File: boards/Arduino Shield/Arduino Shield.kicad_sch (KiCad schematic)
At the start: 21 parts, among them J1 Screw_Terminal_01x08, J11 Screw_Terminal_01x08, J12 Screw_Terminal_01x06, J2 Screw_Terminal_01x08, J3 Screw_Terminal_01x08, J4 Screw_Terminal_01x08, J5 Screw_Terminal_01x08, J6 Screw_Terminal_01x08, J7 Screw_Terminal_01x08, J9 Screw_Terminal_01x10, U1 A000062

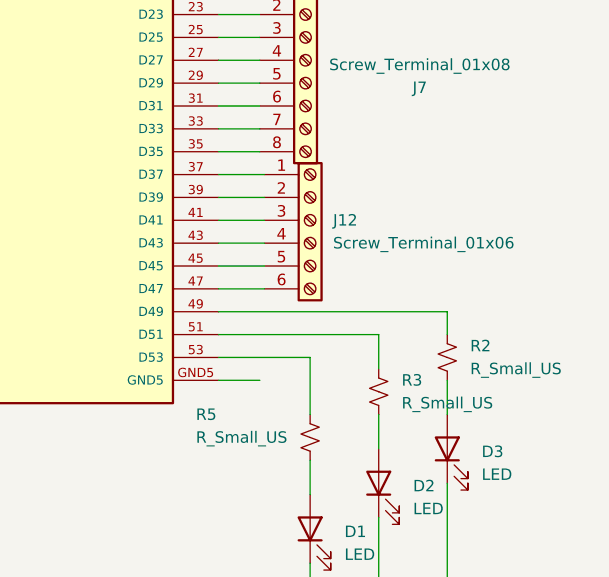
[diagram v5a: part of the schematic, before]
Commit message: Added LEDs and Ground
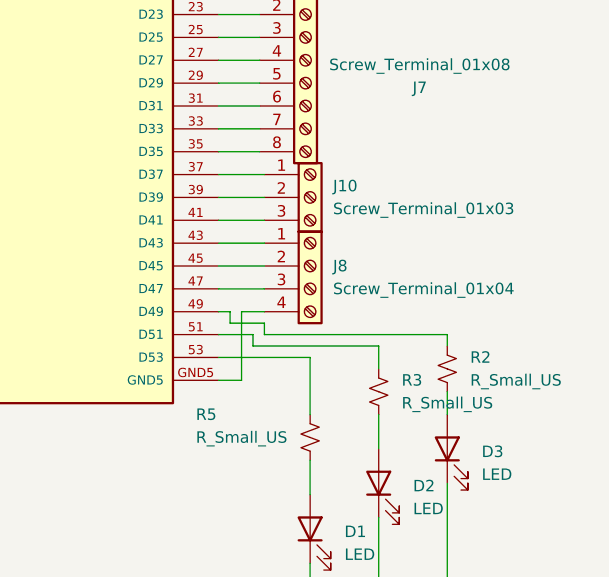
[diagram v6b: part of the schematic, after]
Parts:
- removed J12: Screw_Terminal_01x06, symbol Connector:Screw_Terminal_01x06
- added J10: Screw_Terminal_01x03, symbol Connector:Screw_Terminal_01x03
- added J8: Screw_Terminal_01x04, symbol Connector:Screw_Terminal_01x04
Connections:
- net at U1.37 (D37): now also J10.1 (Pin_1)
- net at U1.39 (D39): now also J10.2 (Pin_2)
- net at U1.41 (D41): now also J10.3 (Pin_3)
- net at U1.43 (D43): now also J8.1 (Pin_1)
- net at U1.45 (D45): now also J8.2 (Pin_2)
- net at U1.47 (D47): now also J8.3 (Pin_3)
- net at U1.GND5: now also J8.4 (Pin_4)
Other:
- moved on the sheet: R2
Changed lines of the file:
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@@
+    (stroke (width 0) (type default))
+  )
+  (wire (pts (xy 148.59 137.16) (xy 148.59 138.43))
     (stroke (width 0) (type default))
   )
@@
     (stroke (width 0) (type default))
   )
+  (wire (pts (xy 149.86 137.16) (xy 170.18 137.16))
+    (stroke (width 0) (type default))
+  )
   (wire (pts (xy 84.328 114.3) (xy 88.9 114.3))
     (stroke (width 0) (type default))
@@
     (stroke (width 0) (type default))
   )
-  (wire (pts (xy 144.78 134.62) (xy 170.18 134.62))
-    (stroke (width 0) (type default))
-  )
   (wire (pts (xy 85.09 137.16) (xy 85.09 143.51))
     (stroke (width 0) (type default))
@@
     (stroke (width 0) (type default))
   )
+  (wire (pts (xy 149.86 135.89) (xy 149.86 137.16))
+    (stroke (width 0) (type default))
+  )
+  (wire (pts (xy 147.32 134.62) (xy 149.86 134.62))
+    (stroke (width 0) (type default))
+  )
   (wire (pts (xy 83.82 142.24) (xy 83.82 137.16))
     (stroke (width 0) (type default))
@@
     (stroke (width 0) (type default))
   )
+  (wire (pts (xy 146.05 135.89) (xy 149.86 135.89))
+    (stroke (width 0) (type default))
+  )
   (wire (pts (xy 149.352 76.2) (xy 144.78 76.2))
     (stroke (width 0) (type default))
@@
     (stroke (width 0) (type default))
   )
-  (wire (pts (xy 144.78 142.24) (xy 149.352 142.24))
-    (stroke (width 0) (type default))
-  )
   (wire (pts (xy 144.78 129.54) (xy 149.86 129.54))
     (stroke (width 0) (type default))
@@
     (stroke (width 0) (type default))
   )
+  (wire (pts (xy 146.05 134.62) (xy 146.05 135.89))
+    (stroke (width 0) (type default))
+  )
   (wire (pts (xy 84.328 101.6) (xy 88.9 101.6))
     (stroke (width 0) (type default))
@@
     (stroke (width 0) (type default))
   )
+  (wire (pts (xy 148.59 138.43) (xy 162.56 138.43))
+    (stroke (width 0) (type default))
+  )
   (wire (pts (xy 84.328 93.98) (xy 88.9 93.98))
     (stroke (width 0) (type default))
@@
     (stroke (width 0) (type default))
   )
+  (wire (pts (xy 162.56 138.43) (xy 162.56 140.97))
+    (stroke (width 0) (type default))
+  )
+  (wire (pts (xy 147.32 142.24) (xy 147.32 134.62))
+    (stroke (width 0) (type default))
+  )
   (wire (pts (xy 84.328 38.1) (xy 88.9 38.1))
     (stroke (width 0) (type default))
@@
     (stroke (width 0) (type default))
   )
-  (wire (pts (xy 162.56 137.16) (xy 162.56 140.97))
+  (wire (pts (xy 144.78 134.62) (xy 146.05 134.62))
+    (stroke (width 0) (type default))
+  )
+  (wire (pts (xy 144.78 142.24) (xy 147.32 142.24))
+    (stroke (width 0) (type default))
+  )
+  (wire (pts (xy 170.18 137.16) (xy 170.18 138.43))
     (stroke (width 0) (type default))
   )
@@
     (stroke (width 0) (type default))
   )
-  (wire (pts (xy 144.78 137.16) (xy 162.56 137.16))
-    (stroke (width 0) (type default))
-  )
   (wire (pts (xy 84.328 35.56) (xy 88.9 35.56))
     (stroke (width 0) (type default))
@@
     (stroke (width 0) (type default))
   )
+  (wire (pts (xy 144.78 137.16) (xy 148.59 137.16))
+    (stroke (width 0) (type default))
+  )
   (wire (pts (xy 144.78 132.08) (xy 149.86 132.08))
     (stroke (width 0) (type default))
   )
-  (wire (pts (xy 170.18 142.24) (xy 170.18 146.05))
+  (wire (pts (xy 170.18 143.51) (xy 170.18 146.05))
     (stroke (width 0) (type default))
   )
@@
   )
   (wire (pts (xy 149.352 93.98) (xy 144.78 93.98))
-    (stroke (width 0) (type default))
-  )
-  (wire (pts (xy 170.18 134.62) (xy 170.18 137.16))
     (stroke (width 0) (type default))
   )
@@
     )
   )
+  (symbol (lib_id "Connector:Screw_Terminal_01x04") (at 154.94 129.54 0) (unit 1)
+    (in_bom yes) (on_board yes) (dnp no) (fields_autoplaced)
+    (property "Reference" "J8" (at 157.48 129.54 0)
+      (effects (font (size 1.27 1.27)) (justify left))
+    )
+    (property "Value" "Screw_Terminal_01x04" (at 157.48 132.08 0)
+      (effects (font (size 1.27 1.27)) (justify left))
+    )
+    (property "Footprint" "" (at 154.94 129.54 0)
+      (effects (font (size 1.27 1.27)) hide)
+    )
+    (property "Datasheet" "~" (at 154.94 129.54 0)
+      (effects (font (size 1.27 1.27)) hide)
+    )
+    (pin "1")
+    (pin "2")
+    (pin "3")
+    (pin "4")
+    (instances
+      (project "Arduino Shield"
+        (path "/d32bdb2e-fa3a-461a-9e34-c0053c91b5d5"
+          (reference "J8") (unit 1)
+        )
+      )
+    )
+  )
   (symbol (lib_id "Connector:Screw_Terminal_01x08") (at 79.248 86.36 180) (unit 1)
     (in_bom yes) (on_board yes) (dnp no)
@@
         (path "/d32bdb2e-fa3a-461a-9e34-c0053c91b5d5"
           (reference "R5") (unit 1)
+        )
+      )
+    )
+  )
+  (symbol (lib_id "Connector:Screw_Terminal_01x03") (at 154.94 121.92 0) (unit 1)
+    (in_bom yes) (on_board yes) (dnp no) (fields_autoplaced)
+    (property "Reference" "J10" (at 157.48 120.65 0)
+      (effects (font (size 1.27 1.27)) (justify left))
+    )
+    (property "Value" "Screw_Terminal_01x03" (at 157.48 123.19 0)
+      (effects (font (size 1.27 1.27)) (justify left))
+    )
+    (property "Footprint" "" (at 154.94 121.92 0)
+      (effects (font (size 1.27 1.27)) hide)
+    )
+    (property "Datasheet" "~" (at 154.94 121.92 0)
+      (effects (font (size 1.27 1.27)) hide)
+    )
+    (pin "1")
+    (pin "2")
+    (pin "3")
+    (instances
+      (project "Arduino Shield"
+        (path "/d32bdb2e-fa3a-461a-9e34-c0053c91b5d5"
+          (reference "J10") (unit 1)
         )
       )
@@
     )
   )
-  (symbol (lib_id "Device:R_Small_US") (at 170.18 139.7 180) (unit 1)
-    (in_bom yes) (on_board yes) (dnp no) (fields_autoplaced)
-    (property "Reference" "R2" (at 172.72 138.43 0)
-      (effects (font (size 1.27 1.27)) (justify right))
-    )
-    (property "Value" "R_Small_US" (at 172.72 140.97 0)
-      (effects (font (size 1.27 1.27)) (justify right))
-    )
-    (property "Footprint" "" (at 170.18 139.7 0)
-      (effects (font (size 1.27 1.27)) hide)
-    )
-    (property "Datasheet" "~" (at 170.18 139.7 0)
+  (symbol (lib_id "Device:R_Small_US") (at 170.18 140.97 180) (unit 1)
+    (in_bom yes) (on_board yes) (dnp no) (fields_autoplaced)
+    (property "Reference" "R2" (at 172.72 139.7 0)
+      (effects (font (size 1.27 1.27)) (justify right))
+    )
+    (property "Value" "R_Small_US" (at 172.72 142.24 0)
+      (effects (font (size 1.27 1.27)) (justify right))
+    )
+    (property "Footprint" "" (at 170.18 140.97 0)
+      (effects (font (size 1.27 1.27)) hide)
+    )
+    (property "Datasheet" "~" (at 170.18 140.97 0)
       (effects (font (size 1.27 1.27)) hide)
     )
@@
         )
       )
-    )
-  )
-  (symbol (lib_id "Connector:Screw_Terminal_01x06") (at 154.94 124.46 0) (unit 1)
-    (in_bom yes) (on_board yes) (dnp no) (fields_autoplaced)
-    (property "Reference" "J12" (at 157.48 124.46 0)
-      (effects (font (size 1.27 1.27)) (justify left))
-    )
-    (property "Value" "Screw_Terminal_01x06" (at 157.48 127 0)
-      (effects (font (size 1.27 1.27)) (justify left))
-    )
-    (property "Footprint" "" (at 154.94 124.46 0)
-      (effects (font (size 1.27 1.27)) hide)
-    )
-    (property "Datasheet" "~" (at 154.94 124.46 0)
-      (effects (font (size 1.27 1.27)) hide)
-    )
-    (pin "1")
-    (pin "2")
-    (pin "3")
-    (pin "4")
-    (pin "5")
-    (pin "6")
-    (instances
-      (project "Arduino Shield"
-        (path "/d32bdb2e-fa3a-461a-9e34-c0053c91b5d5"
-          (reference "J12") (unit 1)
-        )
-      )

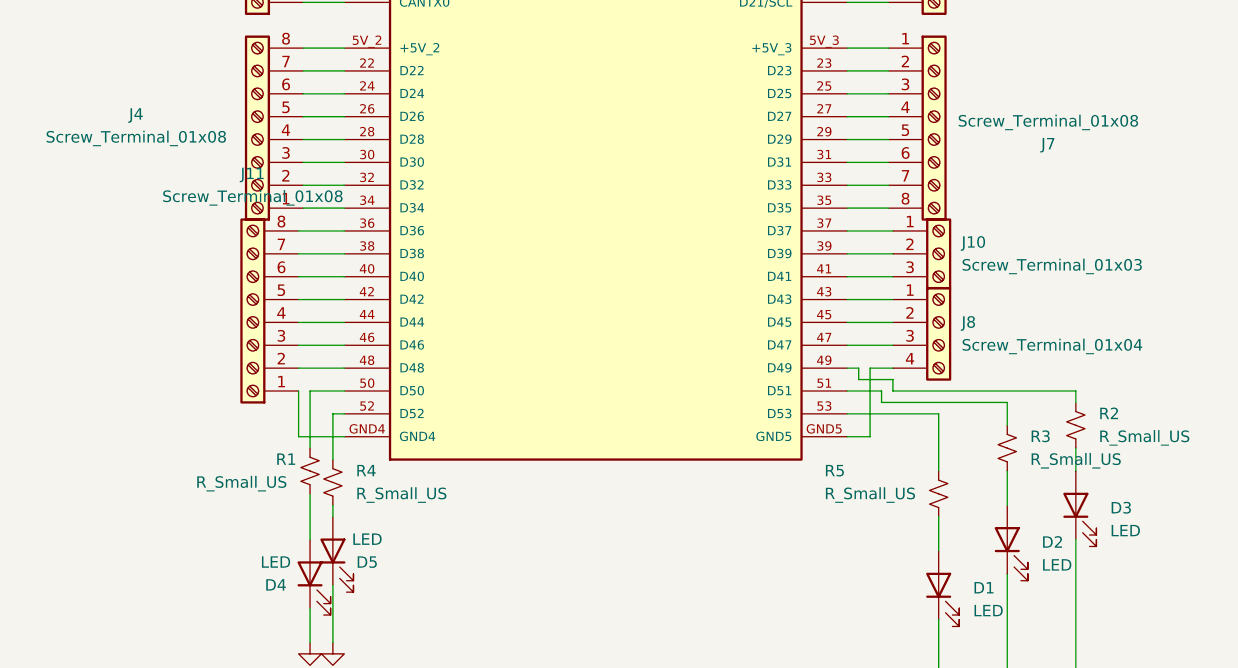
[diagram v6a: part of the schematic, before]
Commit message: Added LEDs with Values
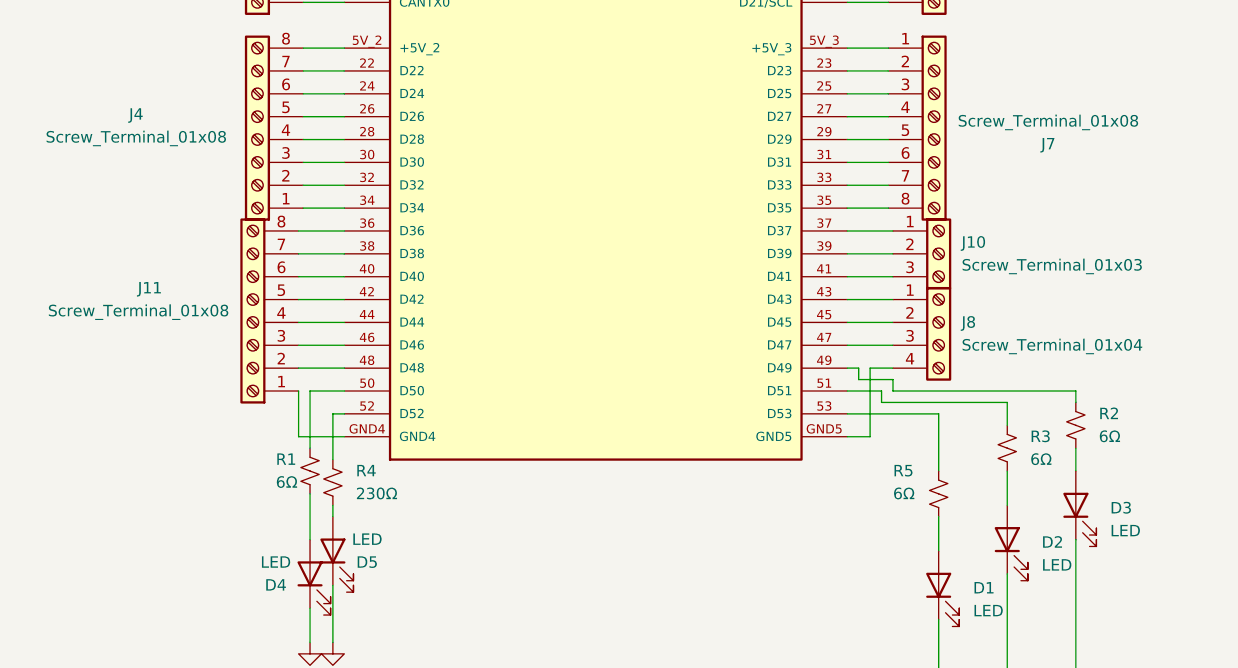
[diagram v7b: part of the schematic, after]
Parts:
- R1, R2, R3, R5: value R_Small_US -> 6Ω
- R4: value R_Small_US -> 230Ω
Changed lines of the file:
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@@
   (symbol (lib_id "Device:R_Small_US") (at 154.94 148.59 180) (unit 1)
     (in_bom yes) (on_board yes) (dnp no)
-    (property "Reference" "R5" (at 142.24 146.05 0)
-      (effects (font (size 1.27 1.27)) (justify right))
-    )
-    (property "Value" "R_Small_US" (at 142.24 148.59 0)
+    (property "Reference" "R5" (at 149.86 146.05 0)
+      (effects (font (size 1.27 1.27)) (justify right))
+    )
+    (property "Value" "6Ω" (at 149.86 148.59 0)
       (effects (font (size 1.27 1.27)) (justify right))
     )
@@
       (effects (font (size 1.27 1.27)) (justify right))
     )
-    (property "Value" "R_Small_US" (at 90.17 148.59 0)
+    (property "Value" "230Ω" (at 90.17 148.59 0)
       (effects (font (size 1.27 1.27)) (justify right))
     )
@@
       (effects (font (size 1.27 1.27)) (justify right))
     )
-    (property "Value" "R_Small_US" (at 172.72 142.24 0)
+    (property "Value" "6Ω" (at 172.72 142.24 0)
       (effects (font (size 1.27 1.27)) (justify right))
     )
@@
       (effects (font (size 1.27 1.27)) hide)
     )
-    (property "Datasheet" "~" (at 87.63 154.94 0)
+    (property "Datasheet" "https://www.mouser.com/datasheet/2/216/APT2012QBC_D-226241.pdf" (at 87.63 154.94 0)
       (effects (font (size 1.27 1.27)) hide)
     )
@@
       (effects (font (size 1.27 1.27)) (justify right))
     )
-    (property "Value" "R_Small_US" (at 165.1 144.78 0)
+    (property "Value" "6Ω" (at 165.1 144.78 0)
       (effects (font (size 1.27 1.27)) (justify right))
     )
@@
       (effects (font (size 1.27 1.27)) (justify right))
     )
-    (property "Value" "R_Small_US" (at 72.39 147.32 0)
+    (property "Value" "6Ω" (at 81.28 147.32 0)
       (effects (font (size 1.27 1.27)) (justify right))
     )
@@
       (effects (font (size 1.27 1.27)) hide)
     )
-    (property "Datasheet" "~" (at 162.56 153.67 0)
+    (property "Datasheet" "https://www.mouser.com/datasheet/2/216/APT2012QBC_D-226241.pdf" (at 162.56 153.67 0)
       (effects (font (size 1.27 1.27)) hide)
     )
@@
       (effects (font (size 1.27 1.27)) hide)
     )
-    (property "Datasheet" "~" (at 154.94 158.75 0)
+    (property "Datasheet" "https://www.mouser.com/datasheet/2/216/APT2012QBC_D-226241.pdf" (at 154.94 158.75 0)
       (effects (font (size 1.27 1.27)) hide)
     )
@@
       (effects (font (size 1.27 1.27)) hide)
     )
-    (property "Datasheet" "~" (at 170.18 149.86 0)
+    (property "Datasheet" "https://www.mouser.com/datasheet/2/216/APT2012QBC_D-226241.pdf" (at 170.18 149.86 0)
       (effects (font (size 1.27 1.27)) hide)
     )
@@
   )
   (symbol (lib_id "Connector:Screw_Terminal_01x08") (at 78.74 129.54 180) (unit 1)
-    (in_bom yes) (on_board yes) (dnp no) (fields_autoplaced)
-    (property "Reference" "J11" (at 78.74 113.03 0)
-      (effects (font (size 1.27 1.27)))
-    )
-    (property "Value" "Screw_Terminal_01x08" (at 78.74 115.57 0)
+    (in_bom yes) (on_board yes) (dnp no)
+    (property "Reference" "J11" (at 67.31 125.73 0)
+      (effects (font (size 1.27 1.27)))
+    )
+    (property "Value" "Screw_Terminal_01x08" (at 66.04 128.27 0)
       (effects (font (size 1.27 1.27)))
     )
@@
       (effects (font (size 1.27 1.27)) hide)
     )
-    (property "Datasheet" "~" (at 85.09 157.48 0)
-      (effects (font (size 1.27 1.27)) hide)
-    )
+    (property "Datasheet" "https://www.mouser.com/datasheet/2/216/APT2012QBC_D-226241.pdf" (at 85.09 157.48 0)
+      (effects (font (size 1.27 1.27)) hide)
+    )

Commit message: Updated pcb
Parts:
- removed J1: Screw_Terminal_01x08, symbol Connector:Screw_Terminal_01x08
- added J1: Screw_Terminal_01x07, TerminalBlock_4Ucon:TerminalBlock_4Ucon_1x07_P3.50mm_Horizontal, symbol Connector:Screw_Terminal_01x07
- D1, D2, D3, D4, D5: footprint (none) -> LED_SMD:LED_0805_2012Metric
- J10: footprint (none) -> TerminalBlock_4Ucon:TerminalBlock_4Ucon_1x03_P3.50mm_Horizontal
- J11, J2, J3, J4, J5, J6, J7: footprint (none) -> TerminalBlock_4Ucon:TerminalBlock_4Ucon_1x08_P3.50mm_Horizontal
- J8: footprint (none) -> TerminalBlock_4Ucon:TerminalBlock_4Ucon_1x04_P3.50mm_Horizontal
- J9: footprint (none) -> TerminalBlock_4Ucon:TerminalBlock_4Ucon_1x10_P3.50mm_Horizontal
- R1, R2, R3, R4, R5: footprint (none) -> Resistor_SMD:R_0805_2012Metric
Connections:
- net at U1.VIN: now also J1.1 (Pin_1)
- net at U1.GND2: now also J1.2 (Pin_2)
- net at U1.GND1: now also J1.3 (Pin_3)
- net at U1.5V_1 (+5V_1): now also J1.4 (Pin_4)
- net at U1.3V3 (+3V3): now also J1.5 (Pin_5)
- net at U1.RESET (~{RESET}): now also J1.6 (Pin_6)
- net at U1.IOREF: now also J1.7 (Pin_7)
